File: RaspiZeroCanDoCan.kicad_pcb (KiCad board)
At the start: 2 copper layers, 21 parts, among them IC1 MCP2562, P6 CAN_conn, P9 CAN_conn, U1 LD1117S50TR, U3 MCP2515-E/ST

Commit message: update pcb
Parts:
- moved C2 25.0 mm to (141.5, 128.0), turned to 180 degrees
- moved OSC1 14.2 mm to (148.5, 126.0), turned to 0 degrees
- moved R4 11.5 mm to (163.0, 110.0), turned to 0 degrees
- moved R5 9.54 mm to (160.5, 112.5), turned to 0 degrees
- moved D4 8.91 mm to (174.5, 110.0), turned to 180 degrees
- moved C4 7.96 mm to (159.5, 128.0)
- moved D1 6.40 mm to (170.0, 112.5), turned to 180 degrees
- moved C5 5.02 mm to (139.0, 124.8)
- moved U3 1.50 mm to (151.9, 118.0)
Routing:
- net CAN_5V: track 37.4 -> 27.5 mm
- net +3V3: track 108.8 -> 102.4 mm
- net Net-(D4-Pad2): track 3.10 -> 9.05 mm
- net GND: track 471.0 -> 476.4 mm
- net Net-(D1-Pad2): track 3.10 -> 7.05 mm
- net CAN_RX: track 17.4 -> 15.9 mm
- net SPI_MISO: track 11.0 -> 9.49 mm
- net INT: track 18.4 -> 16.9 mm
- net SPI_CLK: track 10.5 -> 8.97 mm
- net SPI_MOSI: track 11.8 -> 10.3 mm
- net SPI_CS0: track 19.7 -> 19.0 mm
- net CAN_TX: track 19.4 -> 18.8 mm

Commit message: update pcb
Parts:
- C5: moved to F.Cu
- moved C5 11.5 mm to (146.5, 116.0)
- moved R2 3.54 mm to (147.0, 112.0), turned to 0 degrees
- moved C3 2.50 mm to (142.0, 116.0)
- moved U1 2.50 mm to (140.8, 122.2)
- moved R1 1.12 mm to (147.0, 109.5)
- renumbered D4 to 3v3, D1 to 5v
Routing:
- net GND: track 476.4 -> 468.8 mm
- net CAN_5V: track 27.5 -> 31.0 mm
- net +9V: track 24.1 -> 26.6 mm
- net +3V3: track 102.4 -> 100.6 mm
- net Net-(R2-Pad2): track 4.86 -> 3.60 mm
- net SPI_MOSI: track 10.3 -> 11.2 mm
- net SPI_CS0: track 19.0 -> 18.3 mm
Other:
- board outline added: 65 x 30 mm
- board text added: "PhoenixRobotik '17"
- board text added: "RaspiZeroCanDoCan"
- board text added: "github/PhoenixRobotik/RaspiZeroCanDoCAN"

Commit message: update pcb
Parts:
- moved C2 3.61 mm to (144.5, 126.0)
- moved C4 3.01 mm to (157.2, 126.0)
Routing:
- net GND: track 468.8 -> 462.0 mm
- net Net-(C2-Pad1): track 14.4 -> 10.5 mm
- net Net-(C4-Pad1): track 11.1 -> 8.06 mm
- net +3V3: track 100.6 -> 98.2 mm
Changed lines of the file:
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@@
   (general
     (links 63)
-    (no_connects 1)
-    (area 115.124999 95.3 194.35 132.375001)
+    (no_connects 0)
+    (area 115.924999 101.424999 181.075001 131.575001)
     (thickness 1.6)
     (drawings 13)
-    (tracks 247)
+    (tracks 245)
     (zones 0)
     (modules 21)
@@
   )
   (setup
-    (last_trace_width 0.25)
+    (last_trace_width 0.5)
     (user_trace_width 0.25)
     (user_trace_width 0.35)
@@
   )
   (module Capacitors_SMD:C_0805_HandSoldering (layer B.Cu)
-    (at 141.5 128 180)
+    (at 144.5 126 180)
     (descr "Capacitor SMD 0805, hand soldering")
     (tags "capacitor 0805")
@@
   )
   (module Capacitors_SMD:C_0805_HandSoldering (layer B.Cu)
-    (at 159.5 128)
+    (at 157.25 126)
     (descr "Capacitor SMD 0805, hand soldering")
     (tags "capacitor 0805")
@@
   (segment (start 135 116) (end 135 113) (width 0.5) (layer F.Cu) (net 1) (status 10))
   (segment (start 121 113) (end 129 113) (width 1.5) (layer F.Cu) (net 1) (status 30))
+  (segment (start 143 126.75) (end 143 126) (width 0.25) (layer B.Cu) (net 2))
+  (segment (start 143 127) (end 143 126.75) (width 0.25) (layer B.Cu) (net 2))
+  (segment (start 143 126.75) (end 143 126.25) (width 0.25) (layer B.Cu) (net 2))
+  (segment (start 143 126.25) (end 143.25 126) (width 0.25) (layer B.Cu) (net 2))
+  (segment (start 143 131.003599) (end 143 127) (width 0.25) (layer B.Cu) (net 2))
+  (segment (start 143 131.003599) (end 157.5 131.003599) (width 0.25) (layer B.Cu) (net 2))
+  (segment (start 134 131.003599) (end 143 131.003599) (width 0.25) (layer B.Cu) (net 2))
+  (segment (start 157.5 131.003599) (end 158.5 131.003599) (width 0.25) (layer B.Cu) (net 2))
+  (segment (start 158.5 130.003599) (end 158.5 131.003599) (width 0.25) (layer B.Cu) (net 2))
+  (segment (start 158.5 131.003599) (end 159.5 131.003599) (width 0.25) (layer B.Cu) (net 2))
+  (segment (start 159.5 131.003599) (end 160.5 131.003599) (width 0.25) (layer B.Cu) (net 2))
+  (segment (start 158.5 130.003599) (end 158.5 126) (width 0.25) (layer B.Cu) (net 2))
   (segment (start 143.25 116) (end 145.25 116) (width 0.5) (layer F.Cu) (net 2))
   (segment (start 145.25 116) (end 146.5 117.25) (width 0.5) (layer F.Cu) (net 2))
@@
   (segment (start 154.85 130.853599) (end 155 131.003599) (width 0.35) (layer F.Cu) (net 2))
   (segment (start 160.5 131.003599) (end 174.501101 131.003599) (width 0.25) (layer B.Cu) (net 2))
-  (segment (start 157.5 131.003599) (end 160.5 131.003599) (width 0.25) (layer B.Cu) (net 2))
-  (segment (start 160.5 131.003599) (end 160.75 130.753599) (width 0.25) (layer B.Cu) (net 2))
-  (segment (start 160.75 130.753599) (end 160.75 128) (width 0.25) (layer B.Cu) (net 2))
-  (segment (start 140.25 128) (end 140.25 126.25) (width 0.25) (layer B.Cu) (net 2))
-  (segment (start 140.25 126.25) (end 140 126) (width 0.25) (layer B.Cu) (net 2))
-  (segment (start 140 126) (end 139 126) (width 0.25) (layer B.Cu) (net 2))
-  (segment (start 134 131.003599) (end 157.5 131.003599) (width 0.25) (layer B.Cu) (net 2))
-  (segment (start 140.25 126.75) (end 140.25 128) (width 0.25) (layer B.Cu) (net 2) (status 20))
-  (segment (start 138.5 126) (end 139.5 126) (width 0.25) (layer B.Cu) (net 2) (status 10))
-  (segment (start 134 131.003599) (end 134 126.5) (width 0.25) (layer B.Cu) (net 2))
-  (segment (start 134 126.5) (end 134.5 126) (width 0.25) (layer B.Cu) (net 2))
-  (segment (start 134.5 126) (end 138.5 126) (width 0.25) (layer B.Cu) (net 2) (status 20))
   (segment (start 153.277832 102) (end 160 102) (width 0.35) (layer F.Cu) (net 2))
   (segment (start 153.227822 101.94999) (end 153.277832 102) (width 0.35) (layer F.Cu) (net 2))
@@
   (segment (start 119.5964 105.0036) (end 122.6 102) (width 0.35) (layer F.Cu) (net 2))
   (segment (start 121 120.5) (end 129 120.5) (width 1.5) (layer F.Cu) (net 2) (status 30))
-  (segment (start 142.75 128) (end 146.5 128) (width 0.35) (layer B.Cu) (net 3))
-  (segment (start 146.5 128) (end 148.5 126) (width 0.35) (layer B.Cu) (net 3))
+  (segment (start 148.5 126) (end 145.75 126) (width 0.35) (layer B.Cu) (net 3))
   (segment (start 153.55 120.9) (end 153.55 121.975) (width 0.35) (layer F.Cu) (net 3))
   (segment (start 153.55 121.975) (end 150.274999 125.250001) (width 0.35) (layer F.Cu) (net 3))
   (segment (start 150.274999 125.250001) (end 149.249999 125.250001) (width 0.35) (layer F.Cu) (net 3))
   (segment (start 149.249999 125.250001) (end 148.5 126) (width 0.35) (layer F.Cu) (net 3))
-  (segment (start 158.25 128) (end 155.38 128) (width 0.35) (layer B.Cu) (net 4))
-  (segment (start 155.38 128) (end 153.38 126) (width 0.35) (layer B.Cu) (net 4))
+  (segment (start 153.38 126) (end 156 126) (width 0.35) (layer B.Cu) (net 4))
   (segment (start 153.38 126) (end 154.2 125.18) (width 0.35) (layer F.Cu) (net 4))
   (segment (start 154.2 125.18) (end 154.2 120.9) (width 0.35) (layer F.Cu) (net 4))
+  (segment (start 133 123.5) (end 121 123.5) (width 0.5) (layer B.Cu) (net 5))
+  (segment (start 138.905 119.7) (end 138.905 120.975) (width 0.5) (layer B.Cu) (net 5))
+  (segment (start 138.905 120.975) (end 136.38 123.5) (width 0.5) (layer B.Cu) (net 5))
+  (segment (start 136.38 123.5) (end 133 123.5) (width 0.5) (layer B.Cu) (net 5))
   (segment (start 149 115) (end 146.75 115) (width 0.35) (layer F.Cu) (net 5))
   (segment (start 146.75 115) (end 146.5 114.75) (width 0.35) (layer F.Cu) (net 5))
@@
   (segment (start 124.37 106.27) (end 124.37 107.62) (width 0.5) (layer F.Cu) (net 5))
   (segment (start 156.85 110) (end 161.65 110) (width 0.5) (layer F.Cu) (net 5))
-  (segment (start 138.905 119.7) (end 138.905 123.405) (width 0.5) (layer B.Cu) (net 5))
-  (segment (start 138.905 123.405) (end 139 123.5) (width 0.5) (layer B.Cu) (net 5))
   (segment (start 144.65 106.31) (end 144.69 106.27) (width 0.5) (layer F.Cu) (net 5))
-  (segment (start 138.5 123.5) (end 121 123.5) (width 0.5) (layer B.Cu) (net 5))
   (segment (start 121 123.5) (end 119 121.5) (width 0.5) (layer B.Cu) (net 5))
   (segment (start 119 121.5) (end 119 111.5) (width 0.5) (layer B.Cu) (net 5))
@@
   (segment (start 124.23 106.27) (end 124.37 106.27) (width 0.5) (layer B.Cu) (net 5))
   (segment (start 149 115) (end 149 115.5) (width 0.35) (layer F.Cu) (net 5) (status 30))
-  (segment (start 138.905 119.7) (end 138.905 120.975) (width 0.5) (layer B.Cu) (net 5) (status 10))
   (segment (start 138.905 119.7) (end 138.905 120.22) (width 0.5) (layer B.Cu) (net 5) (status 30))
   (segment (start 161.85 112.5) (end 168.9 112.5) (width 0.5) (layer F.Cu) (net 6))

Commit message: fix footprint, diodes names
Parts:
- removed 3v3, 5v: LED PWR, LEDs:LED_0805
- added LED_3v3_1: 3v3, LEDs:LED_0805, F.Cu at (174.5, 110.0)
- added LED_5v_1: 5v, LEDs:LED_0805, F.Cu at (170.0, 112.5)
- R4: value R -> 56R
- R5: value R -> 150R
- U1: footprint TO_SOT_Packages_SMD:SOT-223 -> TO_SOT_Packages_SMD:SOT-223-3Lead_TabPin2
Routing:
- net CAN_5V: track 31.0 -> 37.3 mm
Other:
- board text added: "3v3"
- board text added: "5v"

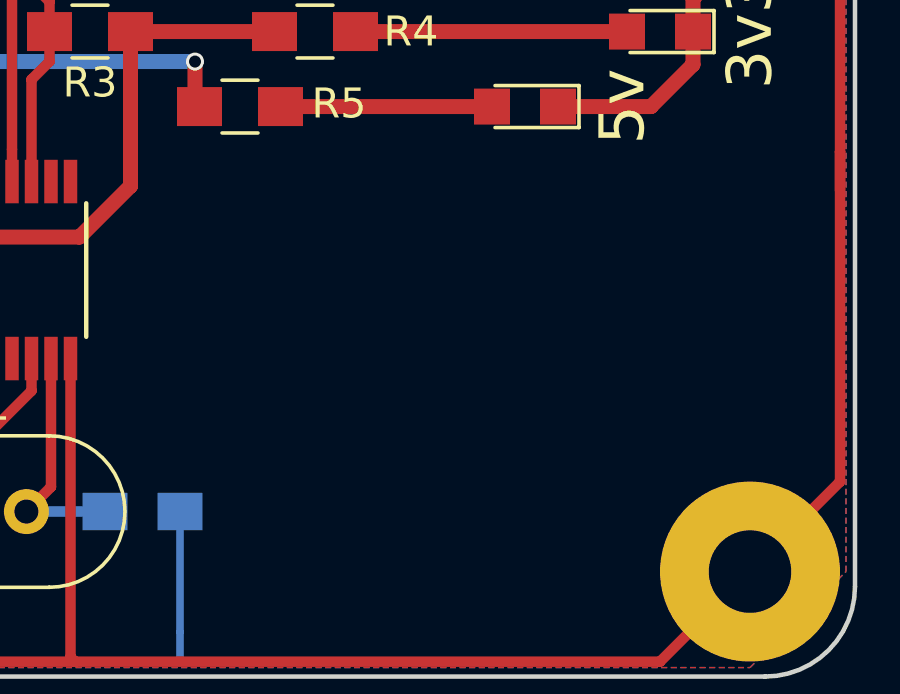
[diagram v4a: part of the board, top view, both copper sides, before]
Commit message: add OSHW logo
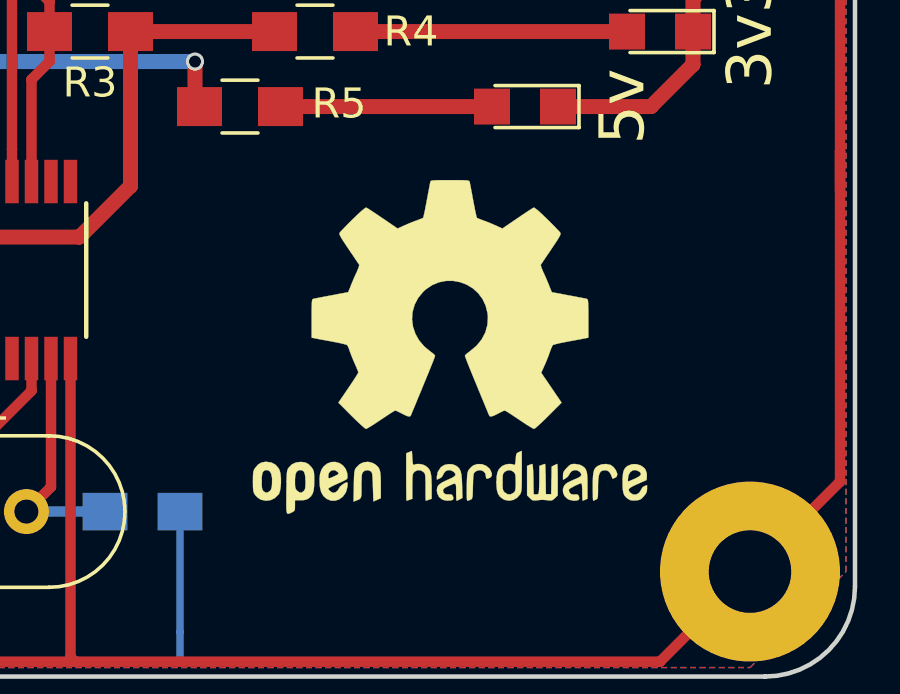
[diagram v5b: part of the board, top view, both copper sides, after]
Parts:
- added REF***: OSHW-Logo2_14.6x12mm_SilkScreen, Symbols:OSHW-Logo2_14.6x12mm_SilkScreen, F.Cu at (167.5, 120.5)

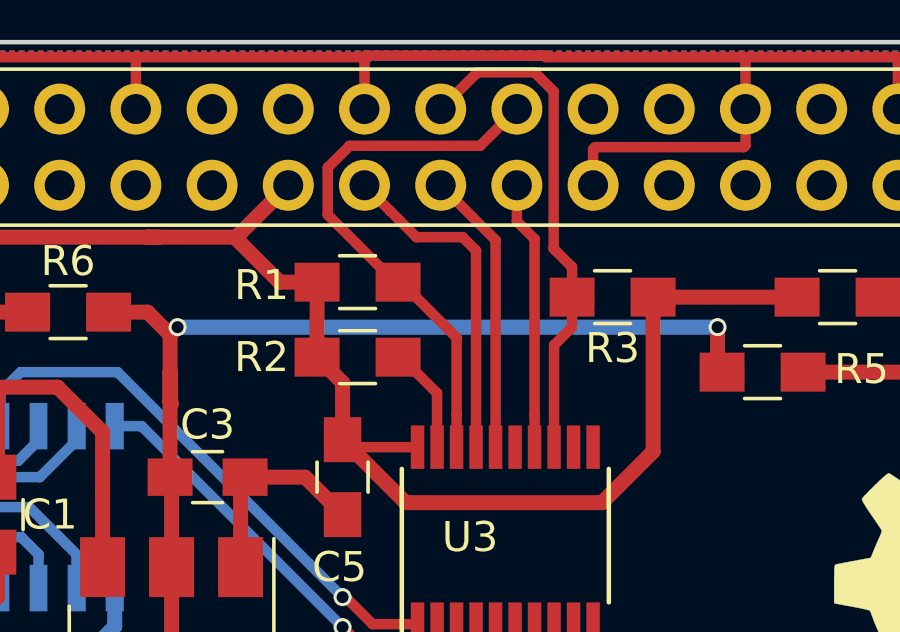
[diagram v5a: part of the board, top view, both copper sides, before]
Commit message: quick fix for MOSI and MISO inversion
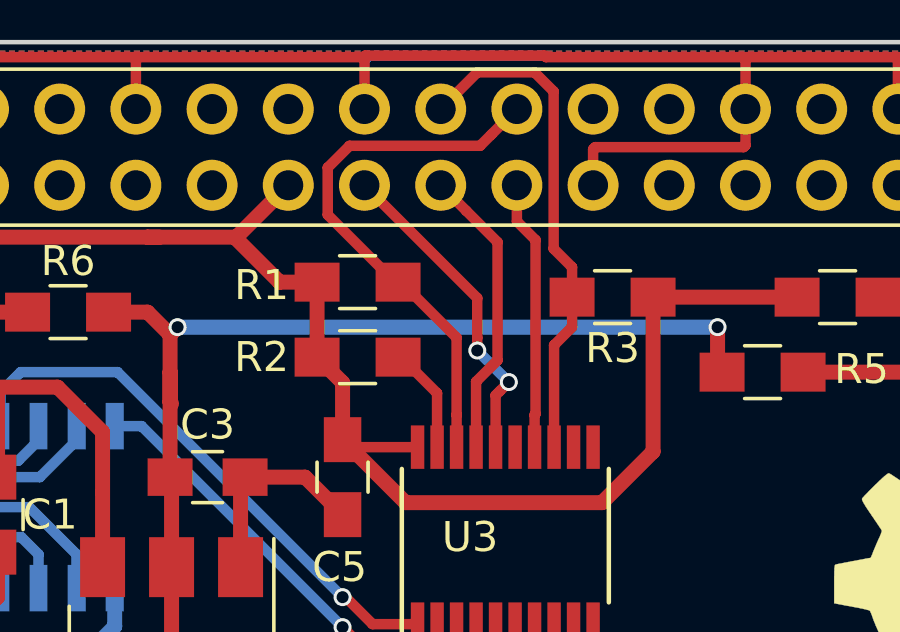
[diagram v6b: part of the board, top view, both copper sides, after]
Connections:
- U3 pad 16: SPI_MISO -> SPI_MOSI
- U3 pad 17: SPI_MOSI -> SPI_MISO
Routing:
- net SPI_MOSI: track 11.2 -> 10.9 mm, vias 0 -> 2
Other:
- net class Default: trace_width 0.25 -> 0.35
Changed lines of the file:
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@@
 (kicad_pcb (version 4) (host pcbnew 4.0.6)
   (general
-    (links 0)
+    (links 64)
     (no_connects 0)
     (area 115.924999 101.424999 181.075001 131.575001)
     (thickness 1.6)
     (drawings 15)
-    (tracks 246)
+    (tracks 255)
     (zones 0)
     (modules 22)
@@
   )
   (setup
-    (last_trace_width 0.25)
+    (last_trace_width 0.35)
     (user_trace_width 0.25)
     (user_trace_width 0.35)
@@
   (net_class Default "Ceci est la Netclass par défaut"
     (clearance 0.2)
-    (trace_width 0.25)
+    (trace_width 0.35)
     (via_dia 0.6)
     (via_drill 0.4)
@@
       (net 47 "Net-(U3-Pad15)"))
     (pad 16 smd rect (at 2.95 -0.325 90) (size 1.45 0.45) (layers F.Cu F.Paste F.Mask)
+      (net 25 SPI_MOSI))
+    (pad 17 smd rect (at 2.95 -0.975 90) (size 1.45 0.45) (layers F.Cu F.Paste F.Mask)
       (net 26 SPI_MISO))
-    (pad 17 smd rect (at 2.95 -0.975 90) (size 1.45 0.45) (layers F.Cu F.Paste F.Mask)
-      (net 25 SPI_MOSI))
     (pad 18 smd rect (at 2.95 -1.625 90) (size 1.45 0.45) (layers F.Cu F.Paste F.Mask)
       (net 11 SPI_CS0))
@@
   (segment (start 135 116) (end 135 113) (width 0.5) (layer F.Cu) (net 1) (status 10))
   (segment (start 121 113) (end 129 113) (width 1.5) (layer F.Cu) (net 1) (status 30))
+  (segment (start 147.2311 103.7336) (end 147.2311 102.0311) (width 0.35) (layer F.Cu) (net 2))
+  (segment (start 147.2 102) (end 147.25001 101.94999) (width 0.35) (layer F.Cu) (net 2))
+  (segment (start 147.2311 102.0311) (end 147.2 102) (width 0.35) (layer F.Cu) (net 2))
+  (segment (start 147.25001 101.94999) (end 153.227822 101.94999) (width 0.35) (layer F.Cu) (net 2))
+  (segment (start 153.227822 101.94999) (end 153.277832 102) (width 0.35) (layer F.Cu) (net 2))
+  (segment (start 147.2311 102.172501) (end 147.2311 103.7336) (width 0.25) (layer B.Cu) (net 2))
   (segment (start 143 126.75) (end 143 126) (width 0.25) (layer B.Cu) (net 2))
   (segment (start 143 127) (end 143 126.75) (width 0.25) (layer B.Cu) (net 2))
@@
   (segment (start 160.5 131.003599) (end 174.501101 131.003599) (width 0.25) (layer B.Cu) (net 2))
   (segment (start 153.277832 102) (end 160 102) (width 0.35) (layer F.Cu) (net 2))
-  (segment (start 153.227822 101.94999) (end 153.277832 102) (width 0.35) (layer F.Cu) (net 2))
-  (segment (start 147.25001 101.94999) (end 153.227822 101.94999) (width 0.35) (layer F.Cu) (net 2))
-  (segment (start 147.2 102) (end 147.25001 101.94999) (width 0.35) (layer F.Cu) (net 2))
   (segment (start 134.494999 115.450001) (end 135.689999 115.450001) (width 0.35) (layer B.Cu) (net 2))
   (segment (start 134.494999 115.450001) (end 133.75 114.705002) (width 0.35) (layer B.Cu) (net 2))
@@
   (segment (start 159.9311 102.072501) (end 159.9311 103.7336) (width 0.25) (layer B.Cu) (net 2))
   (segment (start 147.4 102.003601) (end 139.5 102.003601) (width 0.25) (layer B.Cu) (net 2))
-  (segment (start 147.2311 102.172501) (end 147.2311 103.7336) (width 0.25) (layer B.Cu) (net 2))
   (segment (start 147.4 102.003601) (end 147.2311 102.172501) (width 0.25) (layer B.Cu) (net 2))
   (segment (start 139.5 102.003601) (end 129.4 102.003601) (width 0.25) (layer B.Cu) (net 2))
@@
   (segment (start 139.6 102) (end 139.6111 102.0111) (width 0.35) (layer F.Cu) (net 2))
   (segment (start 139.6111 102.0111) (end 139.6111 103.7336) (width 0.35) (layer F.Cu) (net 2))
-  (segment (start 147.2311 103.7336) (end 147.2311 102.0311) (width 0.35) (layer F.Cu) (net 2))
-  (segment (start 147.2311 102.0311) (end 147.2 102) (width 0.35) (layer F.Cu) (net 2))
   (segment (start 159.9311 102.0689) (end 160 102) (width 0.35) (layer F.Cu) (net 2))
   (segment (start 119.5011 105.0036) (end 119.5964 105.0036) (width 0.35) (layer F.Cu) (net 2))
@@
   (segment (start 150.3 111.35) (end 150.3 113.925) (width 0.35) (layer F.Cu) (net 11))
   (segment (start 150.3 113.925) (end 150.3 115) (width 0.35) (layer F.Cu) (net 11))
+  (segment (start 151.084999 104.955001) (end 151.460001 104.579999) (width 0.35) (layer F.Cu) (net 11))
+  (segment (start 151.460001 104.579999) (end 152.31 103.73) (width 0.35) (layer F.Cu) (net 11))
+  (segment (start 146.731997 104.955001) (end 151.084999 104.955001) (width 0.35) (layer F.Cu) (net 11))
   (segment (start 146.004999 107.254999) (end 146.004999 105.681999) (width 0.35) (layer F.Cu) (net 11))
   (segment (start 148.35 109.5) (end 148.25 109.5) (width 0.35) (layer F.Cu) (net 11))
   (segment (start 148.25 109.5) (end 146.004999 107.254999) (width 0.35) (layer F.Cu) (net 11))
-  (segment (start 146.731997 104.955001) (end 151.084999 104.955001) (width 0.35) (layer F.Cu) (net 11))
   (segment (start 146.004999 105.681999) (end 146.731997 104.955001) (width 0.35) (layer F.Cu) (net 11))
-  (segment (start 151.084999 104.955001) (end 151.460001 104.579999) (width 0.35) (layer F.Cu) (net 11))
-  (segment (start 151.460001 104.579999) (end 152.31 103.73) (width 0.35) (layer F.Cu) (net 11))
   (segment (start 149.65 113.2) (end 149.65 115) (width 0.35) (layer F.Cu) (net 12))
   (segment (start 149.65 113.2) (end 148.45 112) (width 0.35) (layer F.Cu) (net 12))
@@
   (segment (start 154.15 110) (end 154.15 111) (width 0.35) (layer F.Cu) (net 13) (status 10))
   (segment (start 154.15 111) (end 153.55 111.6) (width 0.35) (layer F.Cu) (net 13))
-  (segment (start 148.079999 107.119999) (end 147.23 106.27) (width 0.35) (layer F.Cu) (net 25))
-  (segment (start 148.96 108) (end 148.079999 107.119999) (width 0.35) (layer F.Cu) (net 25))
-  (segment (start 150.5 108) (end 148.96 108) (width 0.35) (layer F.Cu) (net 25))
-  (segment (start 150.95 108.45) (end 150.5 108) (width 0.35) (layer F.Cu) (net 25))
-  (segment (start 150.95 115) (end 150.95 108.45) (width 0.35) (layer F.Cu) (net 25))
-  (segment (start 151.6 115) (end 151.6 108.1) (width 0.35) (layer F.Cu) (net 26))
-  (segment (start 151.6 108.1) (end 149.77 106.27) (width 0.35) (layer F.Cu) (net 26))
+  (segment (start 151.742674 113.130106) (end 152.042673 112.830107) (width 0.35) (layer F.Cu) (net 25))
+  (segment (start 151.6 113.27278) (end 151.742674 113.130106) (width 0.35) (layer F.Cu) (net 25))
+  (segment (start 151.6 115) (end 151.6 113.27278) (width 0.35) (layer F.Cu) (net 25))
+  (segment (start 152.040083 112.830107) (end 152.042673 112.830107) (width 0.35) (layer B.Cu) (net 25))
+  (segment (start 150.989467 111.779491) (end 152.040083 112.830107) (width 0.35) (layer B.Cu) (net 25))
+  (via (at 152.042673 112.830107) (size 0.6) (drill 0.4) (layers F.Cu B.Cu) (net 25))
+  (segment (start 150.989467 111.355227) (end 150.989467 111.779491) (width 0.35) (layer F.Cu) (net 25))
+  (segment (start 150.989467 110.029467) (end 150.989467 111.355227) (width 0.35) (layer F.Cu) (net 25))
+  (segment (start 147.23 106.27) (end 150.989467 110.029467) (width 0.35) (layer F.Cu) (net 25))
+  (via (at 150.989467 111.779491) (size 0.6) (drill 0.4) (layers F.Cu B.Cu) (net 25))
+  (segment (start 150.619999 107.119999) (end 149.77 106.27) (width 0.35) (layer F.Cu) (net 26))
+  (segment (start 151.664468 108.164468) (end 150.619999 107.119999) (width 0.35) (layer F.Cu) (net 26))
+  (segment (start 151.664468 112.103492) (end 151.664468 108.164468) (width 0.35) (layer F.Cu) (net 26))
+  (segment (start 150.95 112.81796) (end 151.664468 112.103492) (width 0.35) (layer F.Cu) (net 26))
+  (segment (start 150.95 115) (end 150.95 112.81796) (width 0.35) (layer F.Cu) (net 26))
+  (segment (start 152.931778 113.893222) (end 152.9 113.925) (width 0.35) (layer F.Cu) (net 27))
+  (segment (start 152.9 113.925) (end 152.9 115) (width 0.35) (layer F.Cu) (net 27))
+  (segment (start 152.31 107.472081) (end 152.931778 108.093859) (width 0.35) (layer F.Cu) (net 27))
   (segment (start 152.31 106.27) (end 152.31 107.472081) (width 0.35) (layer F.Cu) (net 27))
-  (segment (start 152.31 107.472081) (end 152.9 108.062081) (width 0.35) (layer F.Cu) (net 27))
-  (segment (start 152.9 108.062081) (end 152.9 113.925) (width 0.35) (layer F.Cu) (net 27))
-  (segment (start 152.9 113.925) (end 152.9 115) (width 0.35) (layer F.Cu) (net 27))
+  (segment (start 152.931778 108.093859) (end 152.931778 113.893222) (width 0.35) (layer F.Cu) (net 27))
   (segment (start 140.8 119) (end 140.8 125.3) (width 0.5) (layer F.Cu) (net 48))
   (segment (start 140.75 112.5) (end 140.75 111.25) (width 0.5) (layer F.Cu) (net 48))
